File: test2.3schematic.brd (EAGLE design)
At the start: 52.1 x 35.5 mm, 27 parts, among them IC1 FXLN8371QR1, IC2 OPA4990IDR, IC3 ICL7660CSA+, IC4 MAX25210ATAB9_V+, J1 2-1445057-5

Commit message: Test change to verify functionality
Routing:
- net V_3.3V: track 68.5 -> 69.2 mm
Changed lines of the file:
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@@
 <wire x1="12.2555" y1="21.59" x2="12.5805" y2="21.915" width="0.254" layer="1"/>
 <wire x1="12.5805" y1="21.915" x2="13.79" y2="21.915" width="0.254" layer="1"/>
-<wire x1="17.145" y1="33.655" x2="36.1315" y2="33.655" width="0.254" layer="1"/>
+<wire x1="17.145" y1="33.655" x2="37.4015" y2="33.655" width="0.254" layer="1"/>
 <wire x1="47.8605" y1="23.495" x2="45.531" y2="23.495" width="0.254" layer="1"/>
 <wire x1="45.531" y1="23.495" x2="42.2925" y2="26.7335" width="0.254" layer="1"/>
-<wire x1="42.2925" y1="26.7335" x2="42.2925" y2="27.494" width="0.254" layer="1"/>
-<wire x1="42.2925" y1="27.494" x2="36.1315" y2="33.655" width="0.254" layer="1"/>
+<wire x1="42.2925" y1="26.7335" x2="42.2925" y2="28.764" width="0.254" layer="1"/>
+<wire x1="42.2925" y1="28.764" x2="37.4015" y2="33.655" width="0.254" layer="1"/>
 <wire x1="13.79" y1="20.615" x2="12.7225" y2="20.615" width="0.254" layer="1"/>
 <wire x1="12.7225" y1="20.615" x2="12.2555" y2="21.082" width="0.254" layer="1"/>

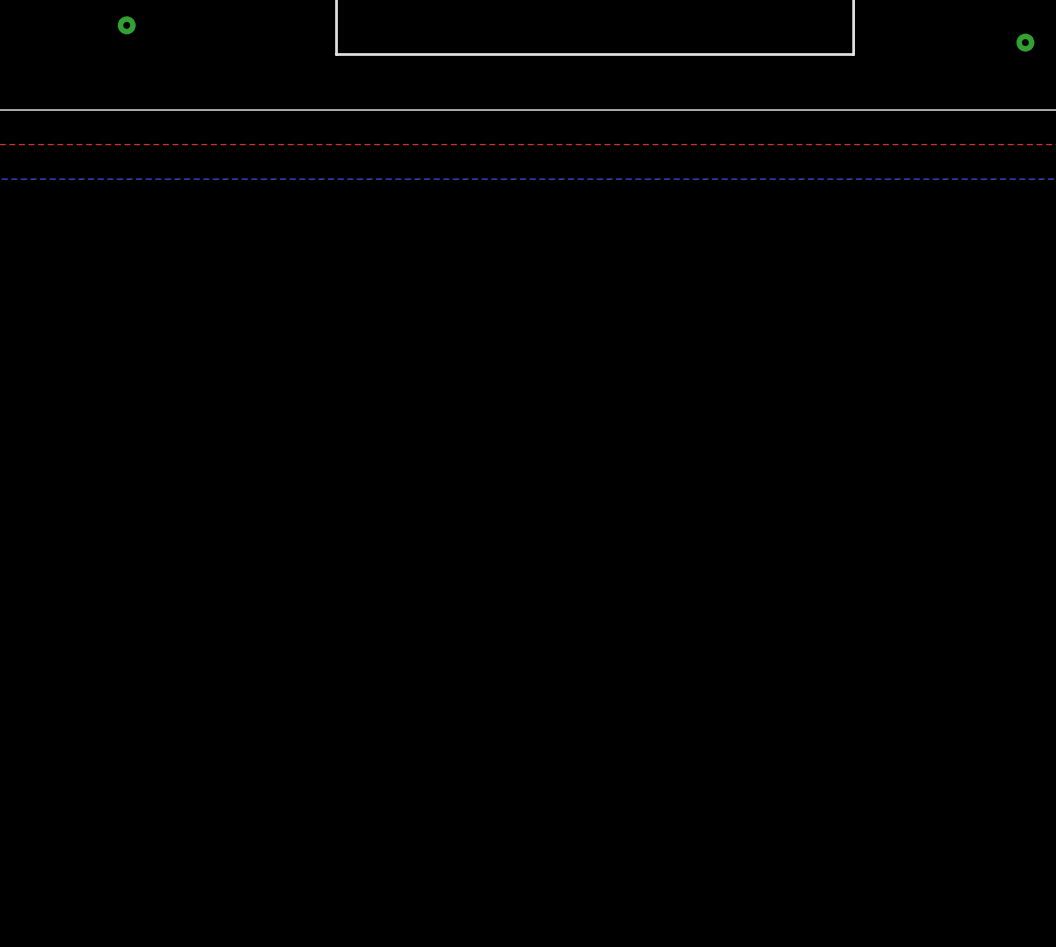
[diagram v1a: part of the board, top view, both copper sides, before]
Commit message: Adding random Connector for testing
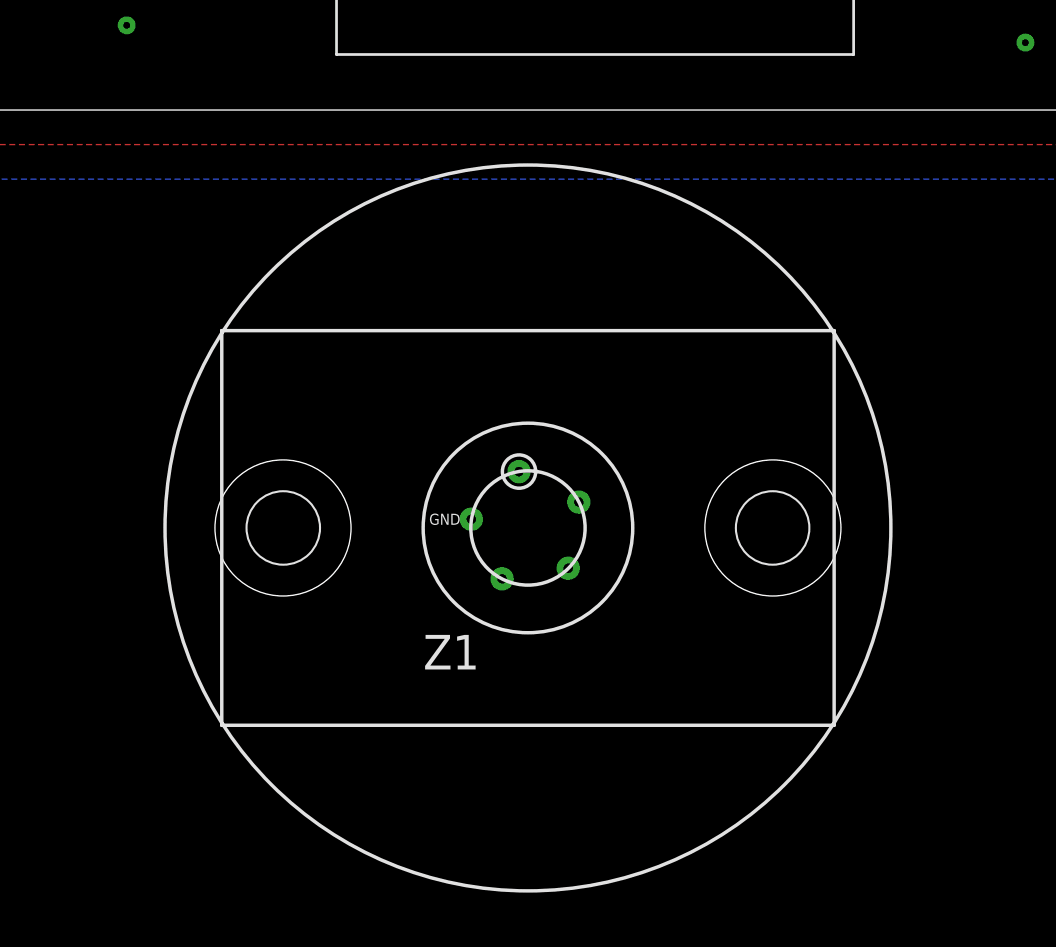
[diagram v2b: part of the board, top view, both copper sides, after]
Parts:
- added Z1: AS_FEMALE_5_PIN, SamacSys_Parts:AS_FEMALE_5_PIN
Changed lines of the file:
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@@
 <attribute name="MOUSER_PRICE-STOCK" value="https://www.mouser.co.uk/ProductDetail/Vishay-Dale/CRCW020110K0FNED?qs=IQLUlsvFoXuh7T4rhkKYcQ%3D%3D" x="10.541" y="23.368" size="1.778" layer="27" display="off"/>
+</element>
+<element name="Z1" library="SamacSys_Parts" package="AS_FEMALE_5_PIN" value="AS_FEMALE_5_PIN" x="12.954" y="-22.606" smashed="yes">
+<attribute name="NAME" x="20.354" y="-20.556" size="1.27" layer="25"/>
+<attribute name="VALUE" x="19.804" y="-11.406" size="1.27" layer="27"/>
 </element>
 </elements>
@@
 packages will not be understood (or retained) with this version.
 </note>
+<note version="8.5" severity="warning">
+Since Version 8.5, EAGLE supports locking for holes, vias, wires and polygons.
+The locking property on all objects of these types will not be understood in this version.
+</note>
 </compatibility>

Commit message: Schematics done and capacitors have 3d packages
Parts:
- removed C10_1UF: 02016D105KAT4A, SamacSys_Parts:CAPC0603X33N
- removed C11_2.2UF: C0402C225Z8VACTU, SamacSys_Parts:INDC1005X55N
- removed C4_8200PF: C0805C822K5RACTU, SamacSys_Parts:CAPC2012X88N
- removed C5_3300PF, C6_3300PF: C0603C332J4GACTU, SamacSys_Parts:CAPC1608X87N
- removed C7_10UF, C8_10UF: 0402X106M6R3CT, SamacSys_Parts:CAPC1005X55N
- removed C9_0.1UF: 06031C104K4Z2A, SamacSys_Parts:CAPC1608X90N
- removed H1, H2, H3, H4: MOUNT-PAD-ROUND3.2, holes:3,2-PAD
- removed IC2: OPA4990IDR, SamacSys_Parts:SOIC127P600X175-14N
- removed IC3: ICL7660CSA+, SamacSys_Parts:SOIC127P600X175-8N
- removed J1: 2-1445057-5, SamacSys_Parts:214450575
- removed R1_10K: CRCW020110K0FNED, SamacSys_Parts:RESC0603X28N
- removed R2_10K_X, R3_10K_Y, R4_10K_Z: CPF-A-0402B10KE, SamacSys_Parts:RESC1005X35N
- removed R2_82.5K_X, R3_82.5K_Y, R4_82.5K_Z: CPF0402B82K5E1, SamacSys_Parts:RESC1005X35N
- removed Z1: AS_FEMALE_5_PIN, SamacSys_Parts:AS_FEMALE_5_PIN
- added C4: CGA5L3X7R1H225K160AB, SamacSys_Parts:CAPC3216X190N
- added C5: CGA6M2X7R1H155K200AA, SamacSys_Parts:CAPC3225X220N
- added C6: CGA5L2C0G1H104J160AA, SamacSys_Parts:CAPC3216X190N
- added C7, C8: CGA3E2C0G1H332J080AA, SamacSys_Parts:CAPC1608X90N
- added IC6: MAX25210ATAB9_V+, SamacSys_Parts:SON65P300X300X80-9N
- added IC7, IC8: NCS21911SN2T1G, SamacSys_Parts:SOT95P275X110-5N
- added JP1: (no value), pinhead:1X05
- added R1, R5, R6: ERA-3ARB182V, SamacSys_Parts:ERA3A_(0603)
- added R2, R3, R4: ERA-2ARB2100X, SamacSys_Parts:ERA2A_(0402)
- added R8: ERJ-PB3B1002V, SamacSys_Parts:RESC1608X55N
- C1: value 0.1uF -> CGA4C2C0G1H822J060AA; device SamacSys_Parts:CAPC1608X90N -> SamacSys_Parts:CAPC2012X75N
- C2: value 4.7uF -> CGA6P3X7R1H475K250AD; device SamacSys_Parts:CAPC2012X135N -> SamacSys_Parts:CGA6P3X7R1H475K250AD
- C3: value 0.1uF -> CGA5L2C0G1H104J160AA; device SamacSys_Parts:CAPC1608X90N -> SamacSys_Parts:CAPC3216X190N
- IC1: value FXLN8371QR1 -> NCS21911SN2T1G; device SamacSys_Parts:QFN65P300X300X100-12N -> SamacSys_Parts:SOT95P275X110-5N
- IC4: value MAX25210ATAB9_V+ -> FXLN8371QR1; device SamacSys_Parts:SON65P300X300X80-9N -> SamacSys_Parts:QFN65P300X300X100-12N
- moved C3 84.1 mm to (-63.1, -14.9)
- moved C2 70.7 mm to (-55.1, -11.2), turned to 0 degrees
- moved IC4 43.5 mm to (-34.3, 2.54)
- moved C1 42.4 mm to (-25.4, 38.1)
- moved IC1 37.9 mm to (-21.6, 12.7)
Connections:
- removed net -VDD: C8_10UF.1, IC2.11, IC3.5
- removed net N$1: C7_10UF.1, IC3.2
- removed net N$2: C7_10UF.2, IC3.4
- removed net X_FEEDBACK: IC2.2, R2_10K_X.1, R2_82.5K_X.1
- removed net Y_FEEDBACK: IC2.6, R3_10K_Y.1, R3_82.5K_Y.1
- removed net Z_FEEDBACK: IC2.9, R4_10K_Z.1, R4_82.5K_Z.1
- new net X-OUT: JP1.3
- net BYP: now also C6.1, IC4.1; no longer C1.1, IC1.1
- net GND: now also C4.2, C5.2, C6.2, C7.2, C8.2, IC1.2, IC4.11, IC4.12, IC4.5, IC6.3, IC6.6, IC6.7, IC7.2, IC8.2, JP1.2, R2.2, R3.2, R4.2; no longer C10_1UF.2, C11_2.2UF.2, C4_8200PF.2, C5_3300PF.2, C6_3300PF.2, C8_10UF.2, C9_0.1UF.2, IC1.11, IC1.12, IC1.3, IC1.5, IC1.6, IC1.7, IC2.12, IC2.13, IC2.14, IC3.3, IC3.6, J1.4, R2_10K_X.2, R3_10K_Y.2, R4_10K_Z.2
- net V_12V: now also C5.1, IC1.5, IC6.1, IC6.2, IC7.5, IC8.5, JP1.1; no longer C10_1UF.1, IC2.4, IC4.1, IC4.2, J1.5
- net V_3.3V: now also C4.1, IC4.2, IC4.4, IC6.8, R8.2; no longer C11_2.2UF.1, C9_0.1UF.1, IC1.2, IC1.4, IC3.8, IC4.8, R1_10K.1
- net V_RESET: now also IC6.4, R8.1; no longer IC4.4, R1_10K.2
- net X_AXIS: now also C8.1, IC1.3, IC4.10; no longer C6_3300PF.1, IC1.10, IC2.3
- net X_OUT: now also IC1.1, IC1.4, R3.1, R6.1, R6.2; no longer IC2.1, J1.1, R2_82.5K_X.2
- net Y_AXIS: now also C7.1, IC4.9, IC7.3; no longer C5_3300PF.1, IC1.9, IC2.5
- net Y_OUT: now also IC7.1, IC7.4, JP1.4, R2.1, R5.1, R5.2; no longer IC2.7, J1.2, R3_82.5K_Y.2
- net Z_AXIS: now also C1.1, IC4.8, IC8.3; no longer C4_8200PF.1, IC1.8, IC2.10
- net Z_OUT: now also IC8.1, IC8.4, JP1.5, R1.1, R1.2, R4.1; no longer IC2.8, J1.3, R4_82.5K_Z.2
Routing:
- net V_3.3V: track 69.2 -> 0.19 mm
- net V_12V: track 61.5 -> 1.72 mm, vias 2 -> 0
- net Y_OUT: track 36.4 -> 0.00 mm, vias 2 -> 0
- net X_OUT: track 27.2 -> 0.00 mm
- net -VDD: track 22.9 -> 0.00 mm, vias 2 -> 0
- net X_AXIS: track 21.5 -> 0.00 mm, vias 2 -> 0
- net Z_AXIS: track 18.0 -> 0.00 mm
- net Y_AXIS: track 16.9 -> 0.00 mm
- net V_RESET: track 12.9 -> 0.00 mm, vias 2 -> 0
- net Z_OUT: track 8.93 -> 0.00 mm
- net N$1: track 8.57 -> 0.00 mm
- net Z_FEEDBACK: track 8.00 -> 0.00 mm
- net Y_FEEDBACK: track 7.08 -> 0.00 mm
- net X_FEEDBACK: track 6.06 -> 0.00 mm
- net GND: track 4.46 -> 9.32 mm, vias 36 -> 1
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- removed copper zone on layer 1, net GND
- removed copper zone on layer 16, net GND
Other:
- board size 52.1 x 35.5 mm -> 160 x 100 mm
- board text removed: "*This board will be epoxied around connectors*"
- board text removed: "12V"
- board text removed: "8g Accelerometer rev 1.1"
- board text removed: "GND"
- board text removed: "Mounting Hole Size: 3.2 mm Date: 5/2021"
- board text removed: "Refer to Baja Google Drive 2020-2021 Folder for part info. Folder for more details"
- board text removed: "X"
- board text removed: "Y"
- board text removed: "Z"
- board text removed: "by Niko Tolentino, CPP BAJA SAE"

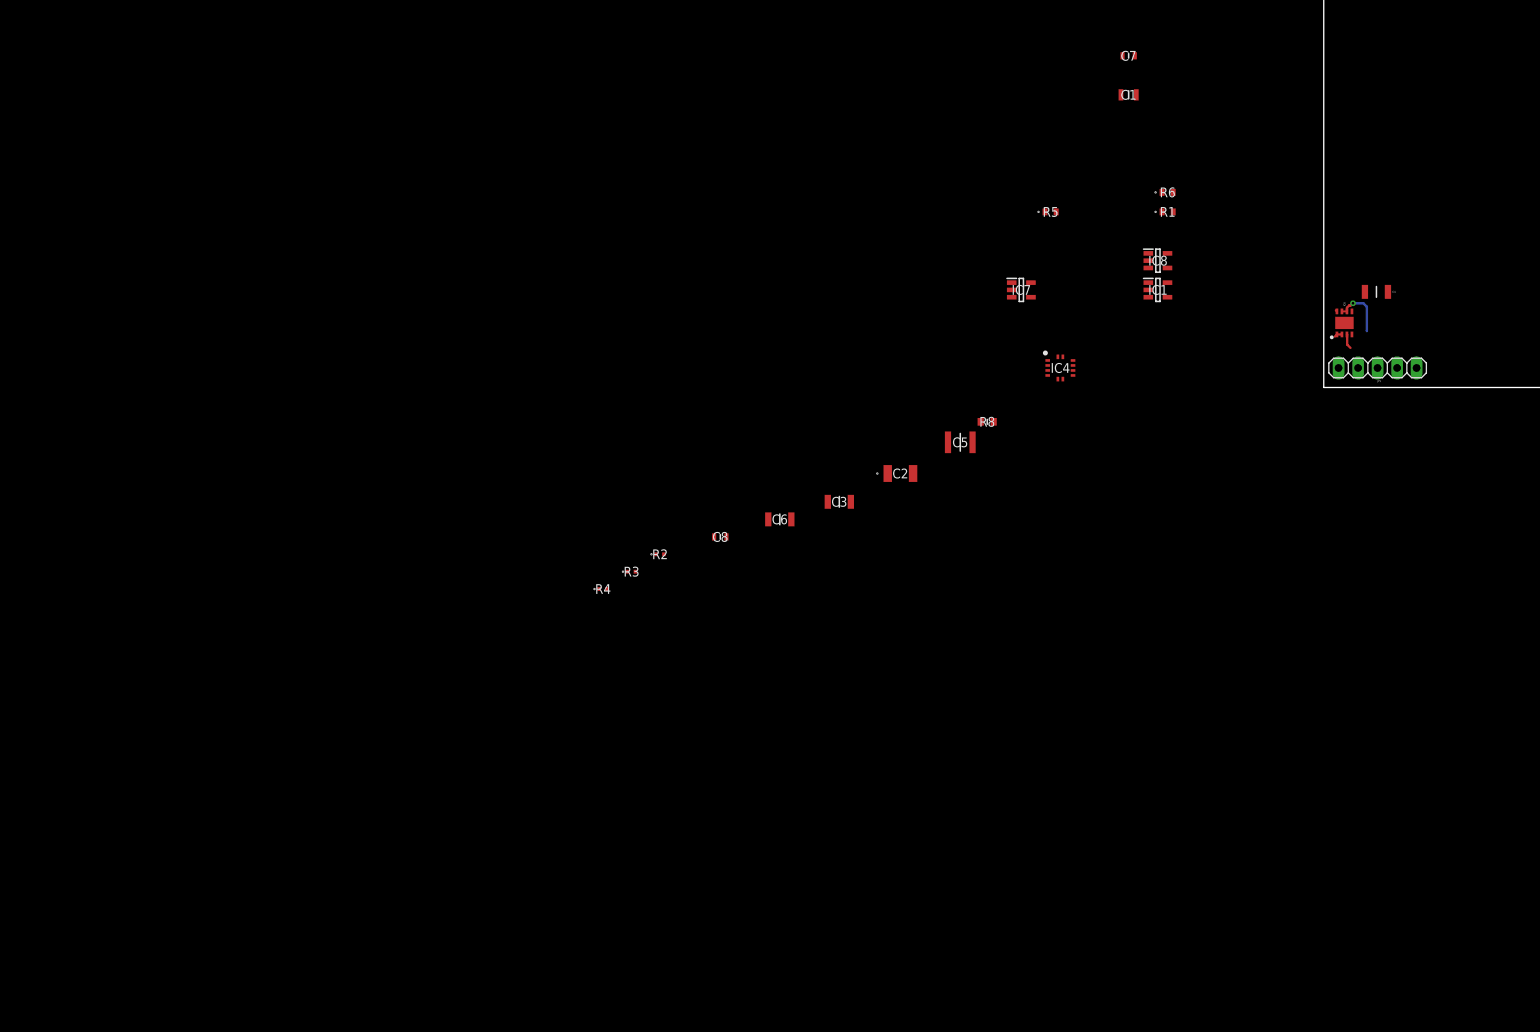
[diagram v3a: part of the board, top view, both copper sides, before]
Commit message: All 3d parts added and Decoupling capacitorss placed on Op amps volatges
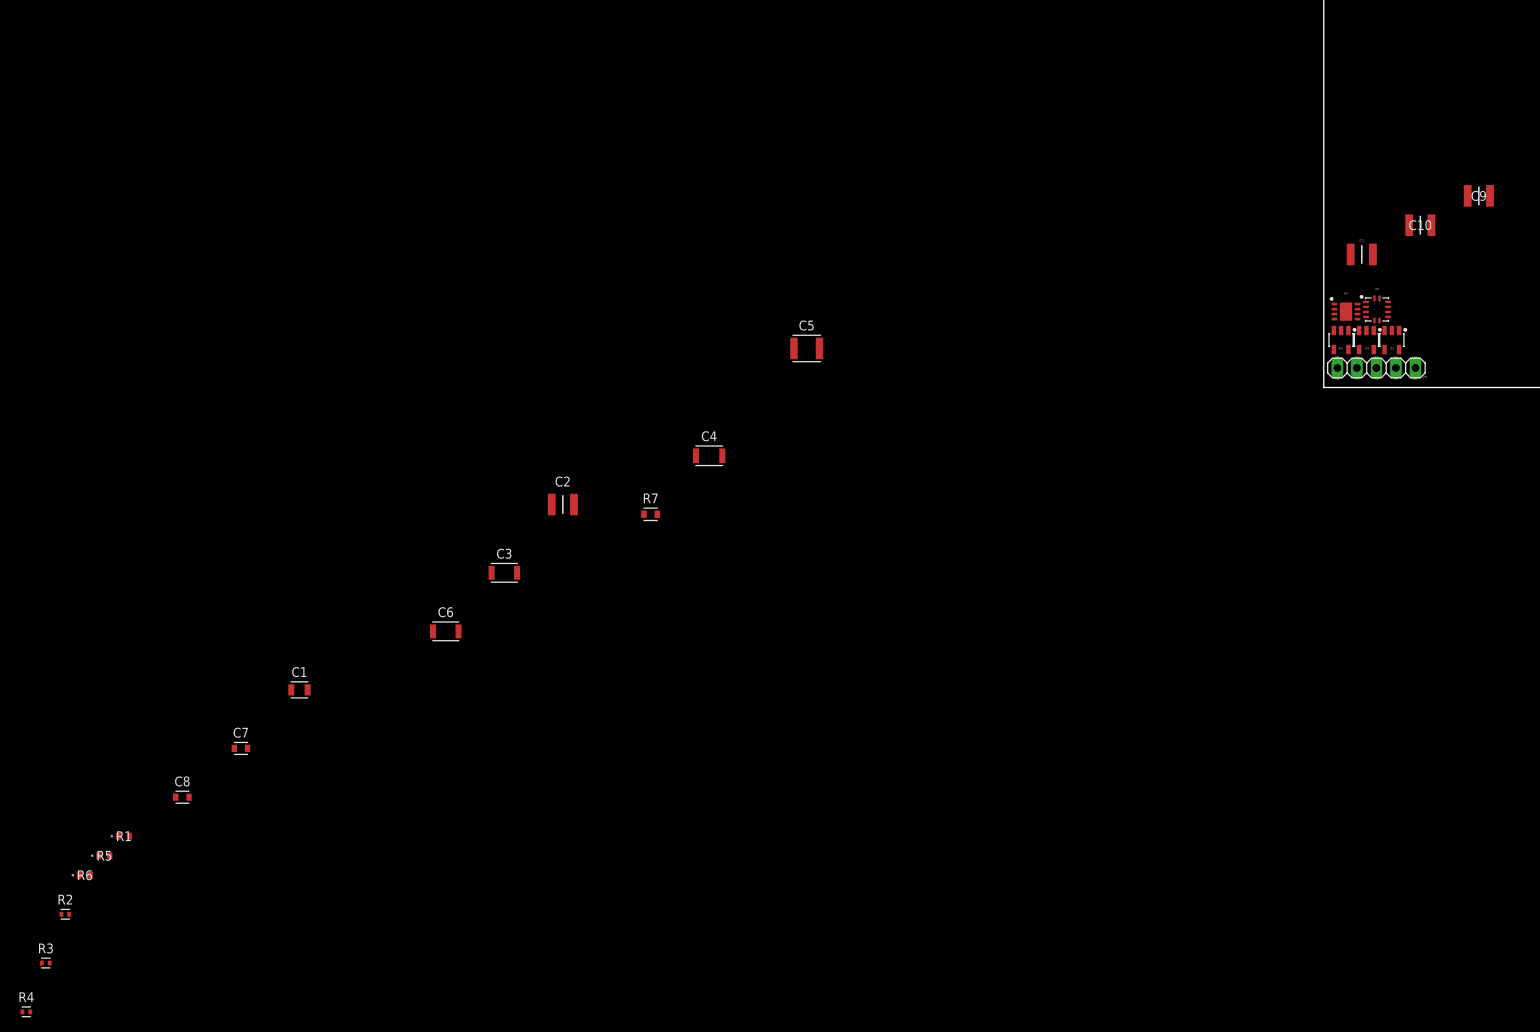
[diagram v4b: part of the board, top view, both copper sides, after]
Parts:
- removed IC6: MAX25210ATAB9_V+, SamacSys_Parts:SON65P300X300X80-9N
- removed IC7, IC8: NCS21911SN2T1G, SamacSys_Parts:SOT95P275X110-5N
- removed R8: ERJ-PB3B1002V, SamacSys_Parts:RESC1608X55N
- added C10, C11, C9: CNA6P1X7R1H475K250AE, SamacSys_Parts:CAPC3225X280N
- added IC2: FXLN8371QR1, SamacSys_Parts:QFN65P300X300X100-12N
- added IC3: MAX25210ATAB9_V+, SamacSys_Parts:SON65P300X300X80-9N
- added IC5: NCS21911SN2T1G, SamacSys_Parts:SOT95P275X110-5N
- added R7: ERJ-PB3B1002V, SamacSys_Parts:RESC1608X55N
- C1: device SamacSys_Parts:CAPC2012X75N -> SamacSys_Parts:CAPC2012X145N
- C2: device SamacSys_Parts:CGA6P3X7R1H475K250AD -> SamacSys_Parts:CAPC3225X280N
- C3, C6: device SamacSys_Parts:CAPC3216X190N -> SamacSys_Parts:CAPC3216X180N
- C4: device SamacSys_Parts:CAPC3216X190N -> SamacSys_Parts:CAPC3317X190N
- IC4: value FXLN8371QR1 -> NCS21911SN2T1G; device SamacSys_Parts:QFN65P300X300X100-12N -> SamacSys_Parts:SOT95P275X110-5N
- R2, R3, R4: device SamacSys_Parts:ERA2A_(0402) -> SamacSys_Parts:RESC1005X40N
- moved R6 166.7 mm to (-161.3, -63.5)
- moved R1 158.3 mm to (-156.2, -58.4)
- moved R5 149.0 mm to (-158.8, -61.0)
- moved C7 146.6 mm to (-141.0, -47.0)
- moved C1 132.9 mm to (-133.3, -39.4)
- moved R4 93.1 mm to (-168.9, -81.3)
- moved R3 91.7 mm to (-166.4, -74.9)
- moved R2 90.5 mm to (-163.8, -68.6)
- moved C4 89.4 mm to (-80.0, -8.89)
- moved C8 77.8 mm to (-148.6, -53.3)
- moved C6 45.9 mm to (-114.3, -31.8)
- moved C3 44.6 mm to (-106.7, -24.1)
- moved C2 44.1 mm to (-99.1, -15.2)
- moved IC4 40.0 mm to (5.56, 6.17), turned to 270 degrees
- moved IC1 31.1 mm to (8.86, 6.17), turned to 270 degrees
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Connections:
- net BYP: now also IC2.1; no longer IC4.1
- net GND: now also C10.2, C11.2, C9.2, IC2.11, IC2.12, IC2.3, IC2.5, IC2.6, IC2.7, IC3.3, IC3.6, IC3.7, IC4.2, IC5.2; no longer IC4.11, IC4.12, IC4.3, IC4.5, IC4.6, IC4.7, IC6.3, IC6.6, IC6.7, IC7.2, IC8.2
- net V_12V: now also C10.1, C11.1, C9.1, IC3.1, IC3.2, IC4.5, IC5.5; no longer IC6.1, IC6.2, IC7.5, IC8.5
- net V_3.3V: now also IC2.2, IC2.4, IC3.8, R7.1; no longer IC4.2, IC4.4, IC6.8, R8.2
- net V_RESET: now also IC3.4, R7.2; no longer IC6.4, R8.1
- net X_AXIS: now also IC2.10; no longer IC4.10
- net X_OUT: now also R2.1; no longer R3.1
- net Y_AXIS: now also IC2.9, IC4.3; no longer IC4.9, IC7.3
- net Y_OUT: now also IC4.1, IC4.4, R3.1; no longer IC7.1, IC7.4, R2.1
- net Z_AXIS: now also IC2.8, IC5.3; no longer IC4.8, IC8.3
- net Z_OUT: now also IC5.1, IC5.4; no longer IC8.1, IC8.4
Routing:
- net GND: track 9.32 -> 0.00 mm, vias 1 -> 0
- net V_12V: track 1.72 -> 0.00 mm

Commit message: Finished The 8G_Accelerometer, awaiting review from FOrrest FOr final revision
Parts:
- moved R4 195.5 mm to (6.60, 4.90), flipped to the bottom, turned to 180 degrees
- moved R3 192.7 mm to (6.55, 10.1), flipped to the bottom, turned to 180 degrees
- moved R2 190.0 mm to (6.60, 15.4), flipped to the bottom, turned to 180 degrees
- moved R6 186.5 mm to (6.65, 17.7), flipped to the bottom, turned to 270 degrees
- moved R5 180.9 mm to (6.63, 12.4), flipped to the bottom, turned to 270 degrees
- moved R1 175.6 mm to (6.63, 7.19), flipped to the bottom, turned to 270 degrees
- moved C8 169.3 mm to (7.77, 11.7)
- moved C7 159.4 mm to (7.77, 10.2)
- moved C1 154.7 mm to (14.4, 6.53), turned to 270 degrees
- moved C6 134.3 mm to (14.5, 6.27), flipped to the bottom, turned to 90 degrees
- moved C3 121.4 mm to (10.6, 7.29), flipped to the bottom, turned to 270 degrees
- moved C2 112.8 mm to (10.5, 11.8), flipped to the bottom, turned to 270 degrees
- moved R7 104.4 mm to (11.8, 15.2), turned to 90 degrees
- moved C4 91.9 mm to (8.71, 14.9), turned to 180 degrees
- moved C5 77.1 mm to (8.71, 18.1)
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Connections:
- removed net X-OUT: JP1.3
- net X_OUT: now also JP1.5
- net Z_OUT: now also JP1.3; no longer JP1.5
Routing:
- net X_OUT: track 0.00 -> 39.8 mm
- net Y_OUT: track 0.00 -> 39.2 mm
- net V_12V: track 0.00 -> 38.2 mm, vias 0 -> 4
- net V_3.3V: track 0.00 -> 24.5 mm, vias 0 -> 3
- net Z_OUT: track 0.00 -> 17.8 mm
- net Z_AXIS: track 0.00 -> 11.1 mm
- net X_AXIS: track 0.00 -> 7.96 mm
- net Y_AXIS: track 0.00 -> 5.02 mm
- net BYP: track 0.00 -> 4.65 mm, vias 0 -> 1
- net V_RESET: track 0.00 -> 3.96 mm, vias 0 -> 1
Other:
- board size 160 x 100 mm -> 18.1 x 22.3 mm

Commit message: Final board done, maybe for feedback from Forrest
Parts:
- moved C6 1.68 mm to (12.9, 6.71)
- moved C1 1.43 mm to (12.9, 6.71)
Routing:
- net X_OUT: track 39.8 -> 36.7 mm
- net V_3.3V: track 24.5 -> 21.5 mm
- net Z_AXIS: track 11.1 -> 9.03 mm
- net BYP: track 4.65 -> 3.49 mm
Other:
- board size 18.1 x 22.3 mm -> 16.4 x 22.3 mm

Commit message: Final Design waiting for Forrest's Analysis - Subject to changes
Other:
- board text added: "X_O"
- board text added: "Y_O"
- board text added: "Z_O"
